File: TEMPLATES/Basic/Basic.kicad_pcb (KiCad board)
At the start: 2 copper layers, 2 parts, among them U1 CpE-3004_LP2985_LDO_1v8

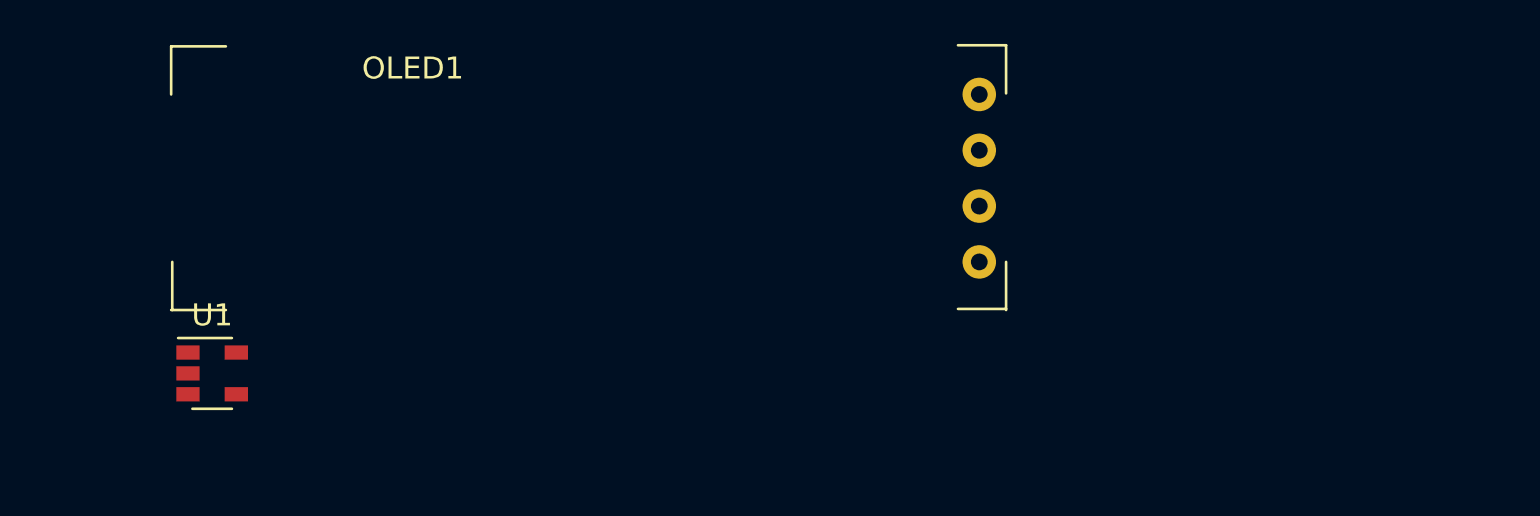
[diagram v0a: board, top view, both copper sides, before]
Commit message: Added PCIe-x4 template
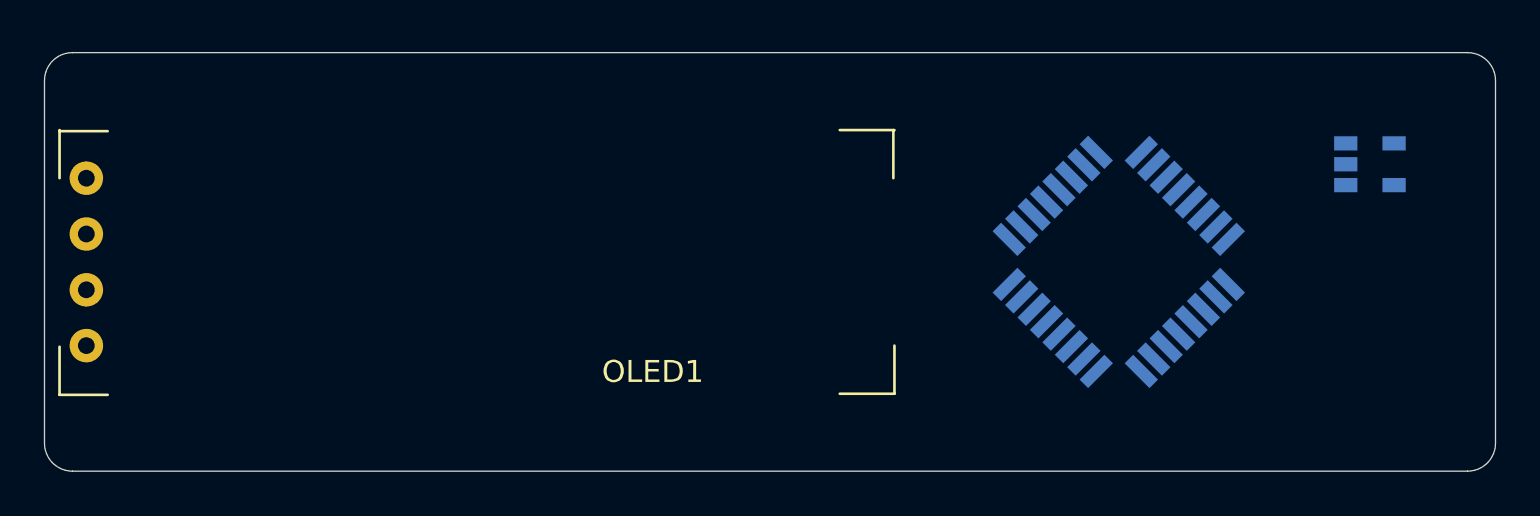
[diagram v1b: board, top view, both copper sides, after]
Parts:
- added U2: ATmega328P-AU, Package_QFP:TQFP-32_7x7mm_P0.8mm, B.Cu at (200.7, 95.2)
- U1: moved to B.Cu
- moved U1 53.5 mm to (212.1, 90.8)
- moved OLED1 40.8 mm to (153.7, 95.2), turned to 180 degrees
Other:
- board outline added: 66 x 19.1 mm
- board text added: "> Connectors for battery, charger, pump, solenoid, and keypad > How does PCB mount into enclosure? >"
